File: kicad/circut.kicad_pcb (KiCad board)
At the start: 2 copper layers, 17 parts, among them J1 AudioOut, J2 AudioOut, J3 I2C, J4 I2C, J5 Input1, J6 Input2, J7 VDD 5v, J8 Input3, J9 Input4, K1 G6K-2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

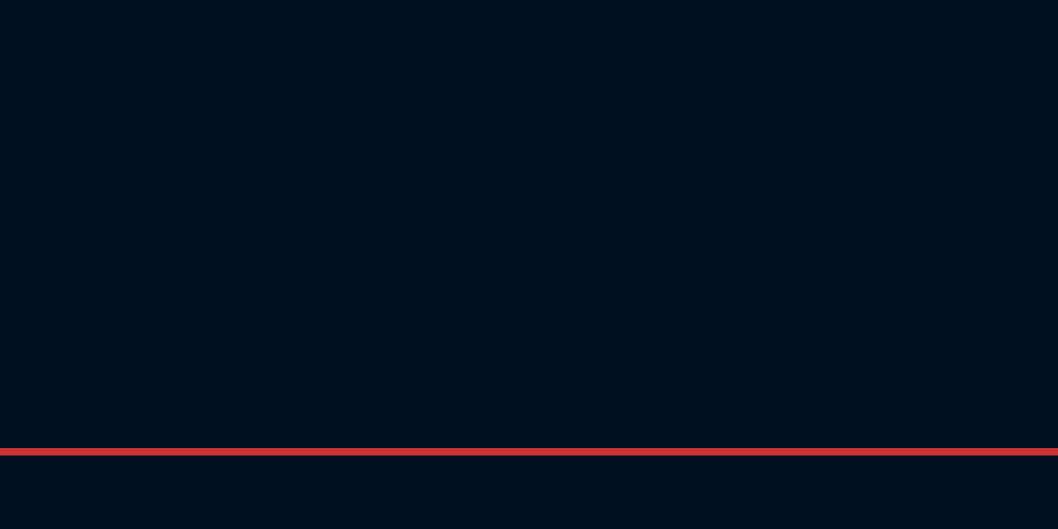
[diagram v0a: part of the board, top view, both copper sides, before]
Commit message: Added cinch 2x2 symbol and footprint for 1x2 and 2x2
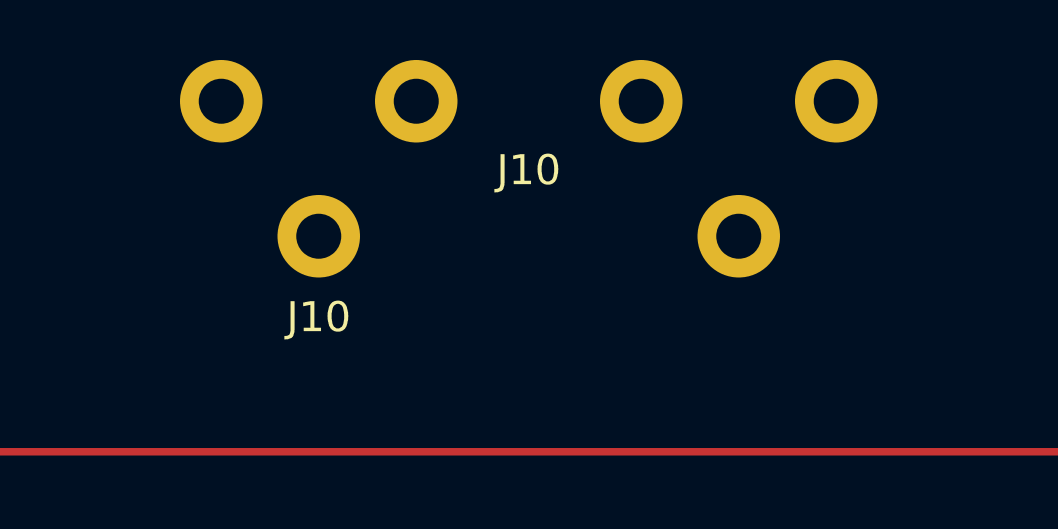
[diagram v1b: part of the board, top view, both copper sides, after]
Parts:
- added J10: Conn_Cinch_2x2, Cinch-Sockets:cinch_2X2_Vertical, F.Cu at (138.4, 58.4)

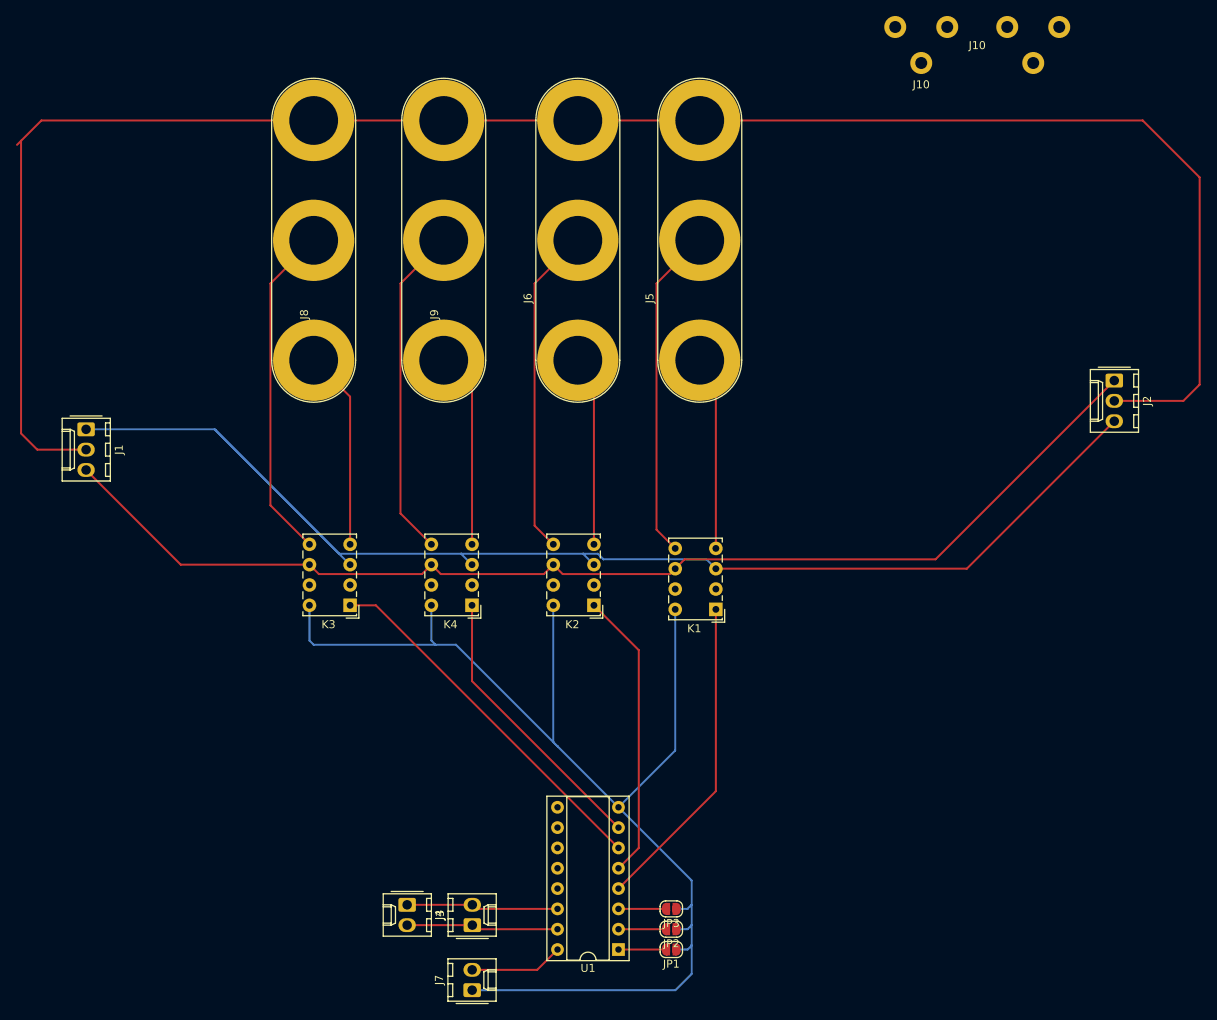
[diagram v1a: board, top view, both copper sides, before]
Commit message: Second PCB Layout - Much smaller. Changed relais wireing.
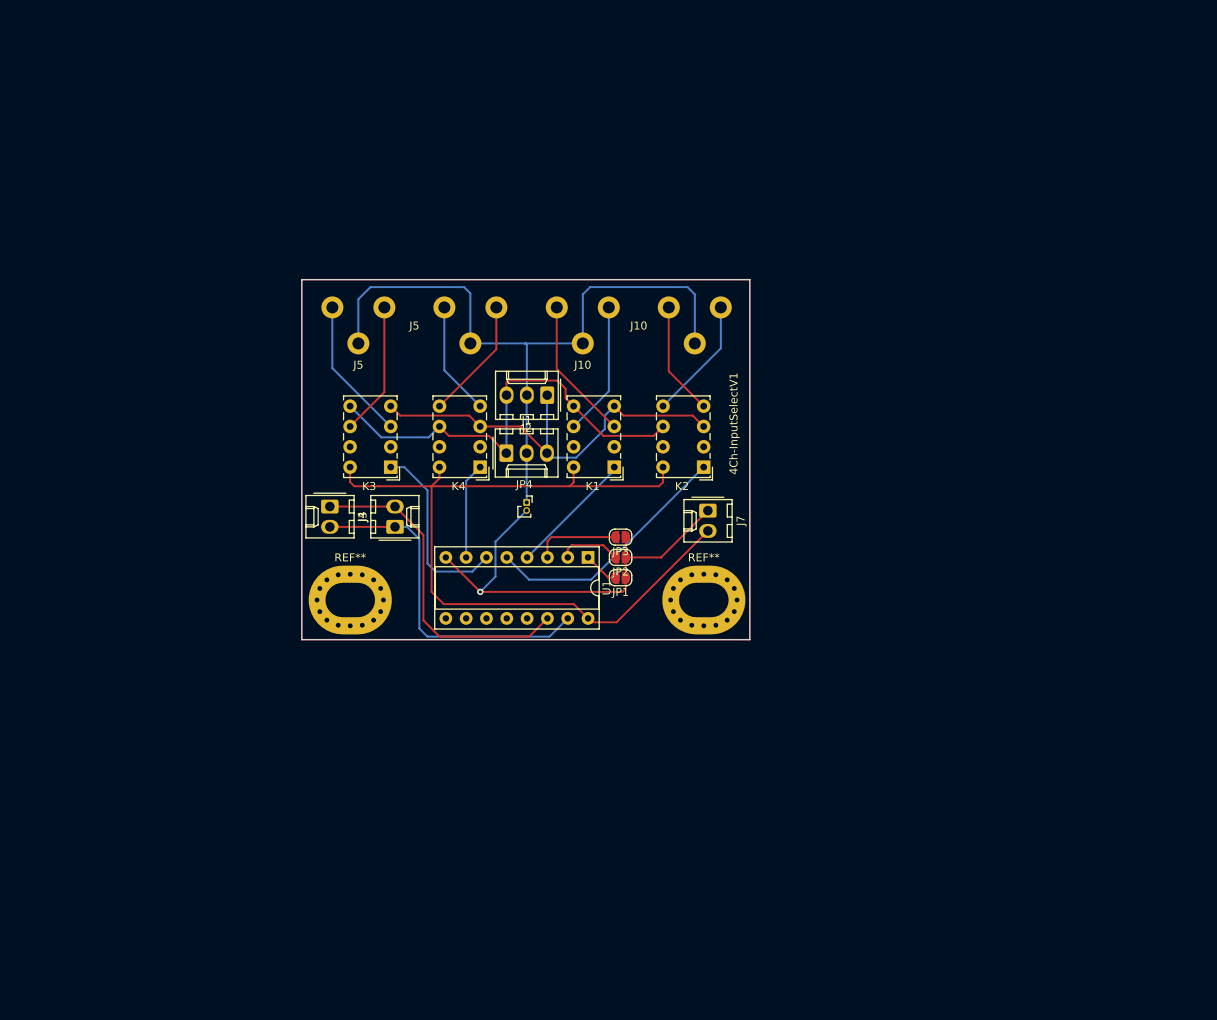
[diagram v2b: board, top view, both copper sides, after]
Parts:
- removed J6: Input2, Connector:Banana_Jack_3Pin
- removed J8: Input3, Connector:Banana_Jack_3Pin
- removed J9: Input4, Connector:Banana_Jack_3Pin
- added JP4: Audio to Control GND, Connector_PinSocket_1.00mm:PinSocket_1x02_P1.00mm_Vertical, F.Cu at (89.1, 117.9)
- added REF**: MountingHole_4.3x6.2mm_M4_Pad_Via, MountingHole:MountingHole_4.3x6.2mm_M4_Pad_Via, F.Cu at (111.3, 130.0)
- added REF**: MountingHole_4.3x6.2mm_M4_Pad_Via, MountingHole:MountingHole_4.3x6.2mm_M4_Pad_Via, F.Cu at (67.1, 130.0)
- J10: value Conn_Cinch_2x2 -> Input 1/2
- J5: value Input1 -> Input 1/2; footprint Connector:Banana_Jack_3Pin -> Cinch-Sockets:cinch_2X2_Vertical
- moved J2 70.9 mm to (91.7, 104.4), turned to 180 degrees
- moved J7 66.8 mm to (111.8, 118.9), turned to -90 degrees
- moved J10 54.9 mm to (96.1, 93.5)
- moved J1 52.6 mm to (86.6, 111.7), turned to 0 degrees
- moved J3 50.7 mm to (64.5, 118.4)
- moved J4 50.7 mm to (72.7, 120.9)
- moved U1 49.2 mm to (96.8, 124.7), turned to -90 degrees
- moved JP3 46.9 mm to (100.8, 122.2)
- moved JP1 46.9 mm to (100.8, 127.3)
- moved JP2 46.9 mm to (100.8, 124.7)
- moved J5 43.2 mm to (68.1, 93.5), turned to 0 degrees
- moved K2 22.1 mm to (111.2, 113.4)
- moved K1 21.8 mm to (100.1, 113.4)
- moved K3 18.0 mm to (72.1, 113.4)
- moved K4 17.3 mm to (83.3, 113.4)
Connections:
- J1 pad 2: Net-(J1-Pad2) -> GND1
- J10 pad 1: Net-(J5-Pad1) -> Net-(J10-Pad1)
- J10 pad 2: Net-(J5-Pad2) -> Net-(J10-Pad2)
- J10 pad 3: Net-(J1-Pad2) -> GND1
- J10 pad 4: Net-(J6-Pad1) -> Net-(J10-Pad4)
- J10 pad 5: Net-(J6-Pad2) -> Net-(J10-Pad5)
- J10 pad 6: Net-(J1-Pad2) -> GND1
- J2 pad 2: Net-(J1-Pad2) -> GND1
- J5 pad 3: Net-(J1-Pad2) -> GND1
- K1 pad 3: Net-(J1-Pad1) -> Net-(J10-Pad2)
- K1 pad 4: Net-(J5-Pad1) -> Net-(J1-Pad3)
- K1 pad 5: Net-(J5-Pad2) -> Net-(J1-Pad1)
- K1 pad 6: Net-(J1-Pad3) -> Net-(J10-Pad1)
- K1 pad 8: GND -> VDD
- K2 pad 3: Net-(J1-Pad1) -> Net-(J1-Pad3)
- K2 pad 4: Net-(J6-Pad1) -> Net-(J10-Pad5)
- K2 pad 5: Net-(J6-Pad2) -> Net-(J10-Pad4)
- K2 pad 6: Net-(J1-Pad3) -> Net-(J1-Pad1)
- K2 pad 8: GND -> VDD
- K3 pad 3: Net-(J1-Pad1) -> Net-(J5-Pad2)
- K3 pad 4: Net-(J8-Pad1) -> Net-(J1-Pad3)
- K3 pad 5: Net-(J8-Pad2) -> Net-(J1-Pad1)
- K3 pad 6: Net-(J1-Pad3) -> Net-(J5-Pad1)
- K3 pad 8: GND -> VDD
- K4 pad 3: Net-(J1-Pad1) -> Net-(J1-Pad3)
- K4 pad 4: Net-(J9-Pad1) -> Net-(J5-Pad5)
- K4 pad 5: Net-(J9-Pad2) -> Net-(J5-Pad4)
- K4 pad 6: Net-(J1-Pad3) -> Net-(J1-Pad1)
- K4 pad 8: GND -> VDD
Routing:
- net Net-(J1-Pad2): track 235.0 -> 0.00 mm
- net Net-(J1-Pad1): track 171.0 -> 55.6 mm
- net GND: track 162.5 -> 56.2 mm, vias 0 -> 1
- net Net-(J1-Pad3): track 145.9 -> 53.7 mm
- net VDD: track 11.7 -> 102.8 mm
- net GND1: track 0.00 -> 87.9 mm
- net Net-(J8-Pad2): track 42.3 -> 0.00 mm
- net Net-(J9-Pad2): track 41.8 -> 0.00 mm
- net Net-(J6-Pad2): track 41.2 -> 0.00 mm
- net Net-(J3-Pad2): track 19.0 -> 44.6 mm
- net Net-(J8-Pad1): track 24.9 -> 0.00 mm
- net Net-(J9-Pad1): track 24.5 -> 0.00 mm
- net Net-(K1-Pad1): track 39.9 -> 15.8 mm
- net Net-(J6-Pad1): track 23.8 -> 0.00 mm
- net Net-(J5-Pad2): track 41.7 -> 17.9 mm
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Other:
- board outline added: 56 x 45 mm
- board text added: "4Ch-InputSelectV1"
